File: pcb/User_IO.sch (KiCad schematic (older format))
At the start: 15 parts, among them P1201 CONN_02X05, P1202 CONN_02X05, SW1201 SW_PUSH, SW1202 SW_PUSH, U401 XC7Axxt-FGG484

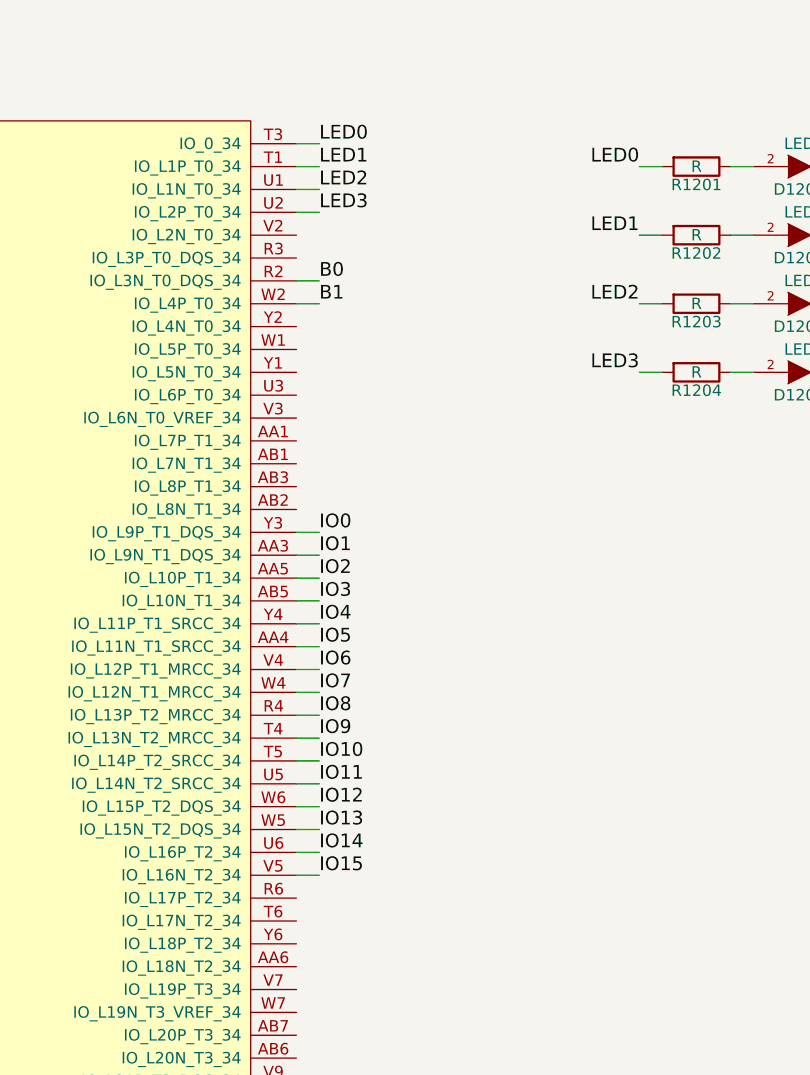
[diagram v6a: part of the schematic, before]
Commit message: routing finished, need final check
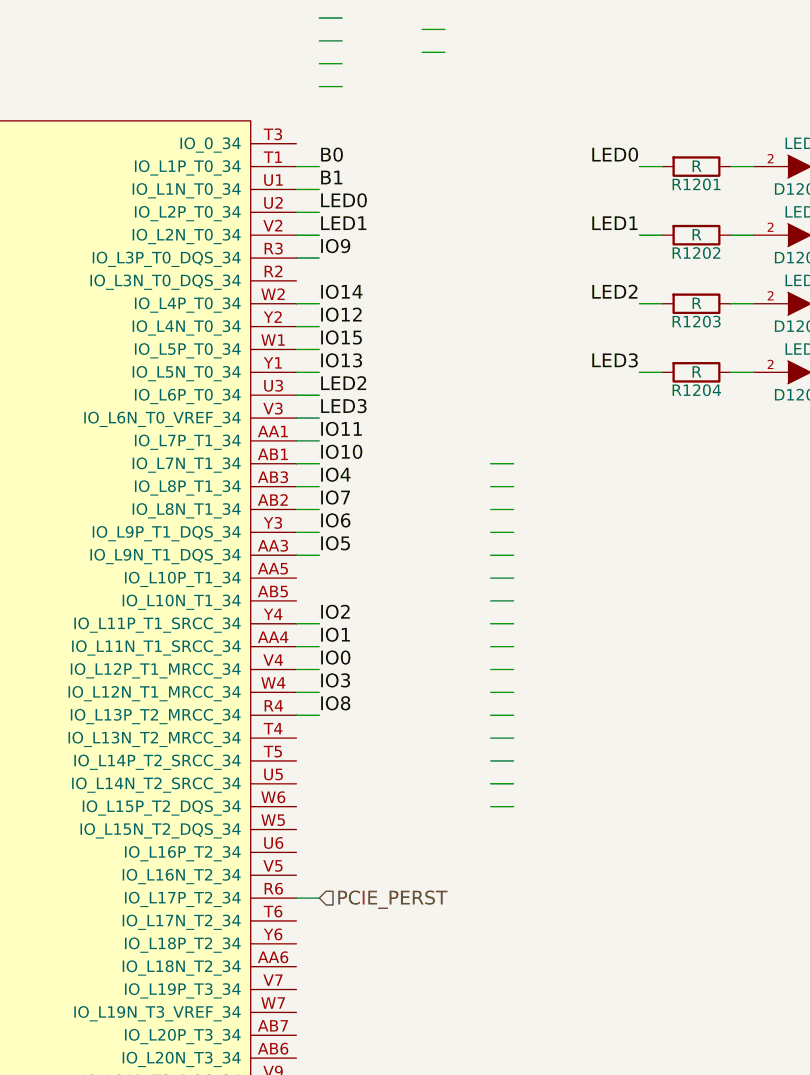
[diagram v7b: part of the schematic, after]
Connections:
- net labels added: PCIE_PERST
- wire segments 67 -> 90
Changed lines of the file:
@@
 $Descr A4 11693 8268
 encoding utf-8
-Sheet 12 11
+Sheet 10 11
 Title ""
 Date ""
@@
 Text Label 6100 2500 2    60   ~ 0
 LED3
-Text Label 4700 1500 0    60   ~ 0
+Text Label 4700 1800 0    60   ~ 0
 LED0
-Text Label 4700 1600 0    60   ~ 0
+Text Label 4700 1900 0    60   ~ 0
 LED1
-Text Label 4700 1700 0    60   ~ 0
+Text Label 4700 2600 0    60   ~ 0
 LED2
-Text Label 4700 1800 0    60   ~ 0
+Text Label 4700 2700 0    60   ~ 0
 LED3
+Text Label 4700 3800 0    60   ~ 0
+IO0
+Text Label 4700 3700 0    60   ~ 0
+IO1
+Text Label 4700 3600 0    60   ~ 0
+IO2
+Text Label 4700 3900 0    60   ~ 0
+IO3
+Text Label 4700 3000 0    60   ~ 0
+IO4
+Text Label 4700 3300 0    60   ~ 0
+IO5
 Text Label 4700 3200 0    60   ~ 0
-IO0
-Text Label 4700 3300 0    60   ~ 0
-IO1
-Text Label 4700 3400 0    60   ~ 0
-IO2
-Text Label 4700 3500 0    60   ~ 0
-IO3
-Text Label 4700 3600 0    60   ~ 0
-IO4
-Text Label 4700 3700 0    60   ~ 0
-IO5
-Text Label 4700 3800 0    60   ~ 0
 IO6
 Text Label 4700 4000 0    60   ~ 0
 IO8
-Text Label 4700 3900 0    60   ~ 0
+Text Label 4700 3100 0    60   ~ 0
 IO7
-Text Label 4700 4100 0    60   ~ 0
+Text Label 4700 2000 0    60   ~ 0
 IO9
-Text Label 4700 4200 0    60   ~ 0
+Text Label 4700 2900 0    60   ~ 0
 IO10
-Text Label 4700 4300 0    60   ~ 0
+Text Label 4700 2800 0    60   ~ 0
 IO11
-Text Label 4700 4400 0    60   ~ 0
+Text Label 4700 2300 0    60   ~ 0
 IO12
-Text Label 4700 4500 0    60   ~ 0
+Text Label 4700 2500 0    60   ~ 0
 IO13
-Text Label 4700 4600 0    60   ~ 0
+Text Label 4700 2200 0    60   ~ 0
 IO14
-Text Label 4700 4700 0    60   ~ 0
+Text Label 4700 2400 0    60   ~ 0
 IO15
 Wire Wire Line
@@
 	6200 2500 6100 2500
 Wire Wire Line
-	4600 1500 4700 1500
-Wire Wire Line
-	4600 1600 4700 1600
-Wire Wire Line
-	4600 1700 4700 1700
-Wire Wire Line
-	4600 1800 4700 1800
-Wire Wire Line
-	4600 3200 4700 3200
-Wire Wire Line
-	4600 3300 4700 3300
-Wire Wire Line
-	4600 3400 4700 3400
-Wire Wire Line
-	4600 3500 4700 3500
-Wire Wire Line
-	4600 3600 4700 3600
-Wire Wire Line
-	4600 3700 4700 3700
-Wire Wire Line
-	4600 3800 4700 3800
-Wire Wire Line
-	4600 3900 4700 3900
-Wire Wire Line
-	4600 4000 4700 4000
-Wire Wire Line
-	4600 4100 4700 4100
-Wire Wire Line
-	4600 4200 4700 4200
-Wire Wire Line
-	4600 4300 4700 4300
-Wire Wire Line
-	4600 4400 4700 4400
-Wire Wire Line
-	4600 4500 4700 4500
-Wire Wire Line
-	4600 4600 4700 4600
-Wire Wire Line
-	4600 4700 4700 4700
+	4700 950  4800 950
+Wire Wire Line
+	4700 1050 4800 1050
+Wire Wire Line
+	4700 1150 4800 1150
+Wire Wire Line
+	4700 1250 4800 1250
+Wire Wire Line
+	5450 2900 5550 2900
+Wire Wire Line
+	5450 3000 5550 3000
+Wire Wire Line
+	5450 3100 5550 3100
+Wire Wire Line
+	5450 3200 5550 3200
+Wire Wire Line
+	5450 3300 5550 3300
+Wire Wire Line
+	5450 3400 5550 3400
+Wire Wire Line
+	5450 3500 5550 3500
+Wire Wire Line
+	5450 3600 5550 3600
+Wire Wire Line
+	5450 3700 5550 3700
+Wire Wire Line
+	5450 3800 5550 3800
+Wire Wire Line
+	5450 3900 5550 3900
+Wire Wire Line
+	5450 4000 5550 4000
+Wire Wire Line
+	5450 4100 5550 4100
+Wire Wire Line
+	5450 4200 5550 4200
+Wire Wire Line
+	5450 4300 5550 4300
+Wire Wire Line
+	5450 4400 5550 4400
 Wire Wire Line
 	7800 3100 7700 3100
@@
 	10000 3700 10000 3900
 Wire Wire Line
-	4600 2100 4700 2100
-Wire Wire Line
-	4600 2200 4700 2200
-Text Label 4700 2100 0    60   ~ 0
+	5150 1000 5250 1000
+Wire Wire Line
+	5150 1100 5250 1100
+Text Label 4700 1600 0    60   ~ 0
 B0
-Text Label 4700 2200 0    60   ~ 0
+Text Label 4700 1700 0    60   ~ 0
 B1
 Text Label 10500 3100 0    60   ~ 0
@@
 Text Label 9800 3100 2    60   ~ 0
 B1
+Text HLabel 4700 4800 2    60   Input ~ 0
+PCIE_PERST
+Wire Wire Line
+	4600 3800 4700 3800
+Wire Wire Line
+	4600 3900 4700 3900
+Wire Wire Line
+	4600 3600 4700 3600
+Wire Wire Line
+	4600 3700 4700 3700
+Wire Wire Line
+	4600 3200 4700 3200
+Wire Wire Line
+	4600 3300 4700 3300
+Wire Wire Line
+	4600 3000 4700 3000
+Wire Wire Line
+	4600 3100 4700 3100
+Wire Wire Line
+	4600 4000 4700 4000
+Wire Wire Line
+	4600 2000 4700 2000
+Wire Wire Line
+	4600 2800 4700 2800
+Wire Wire Line
+	4600 2900 4700 2900
+Wire Wire Line
+	4600 2500 4700 2500
+Wire Wire Line
+	4600 2400 4700 2400
+Wire Wire Line
+	4600 2300 4700 2300
+Wire Wire Line
+	4600 2200 4700 2200
+Wire Wire Line
+	4600 1600 4700 1600
+Wire Wire Line
+	4600 1700 4700 1700
+Wire Wire Line
+	4600 1800 4700 1800
+Wire Wire Line
+	4600 1900 4700 1900
+Wire Wire Line
+	4600 2600 4700 2600
+Wire Wire Line
+	4600 2700 4700 2700
+Wire Wire Line
+	4600 4800 4700 4800
 $EndSCHEMATC
